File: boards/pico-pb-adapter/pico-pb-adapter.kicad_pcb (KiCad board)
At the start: 2 copper layers, 63.5 x 33 mm, 2 parts, among them U1 RPi_Pico, U2 PocketBeagle

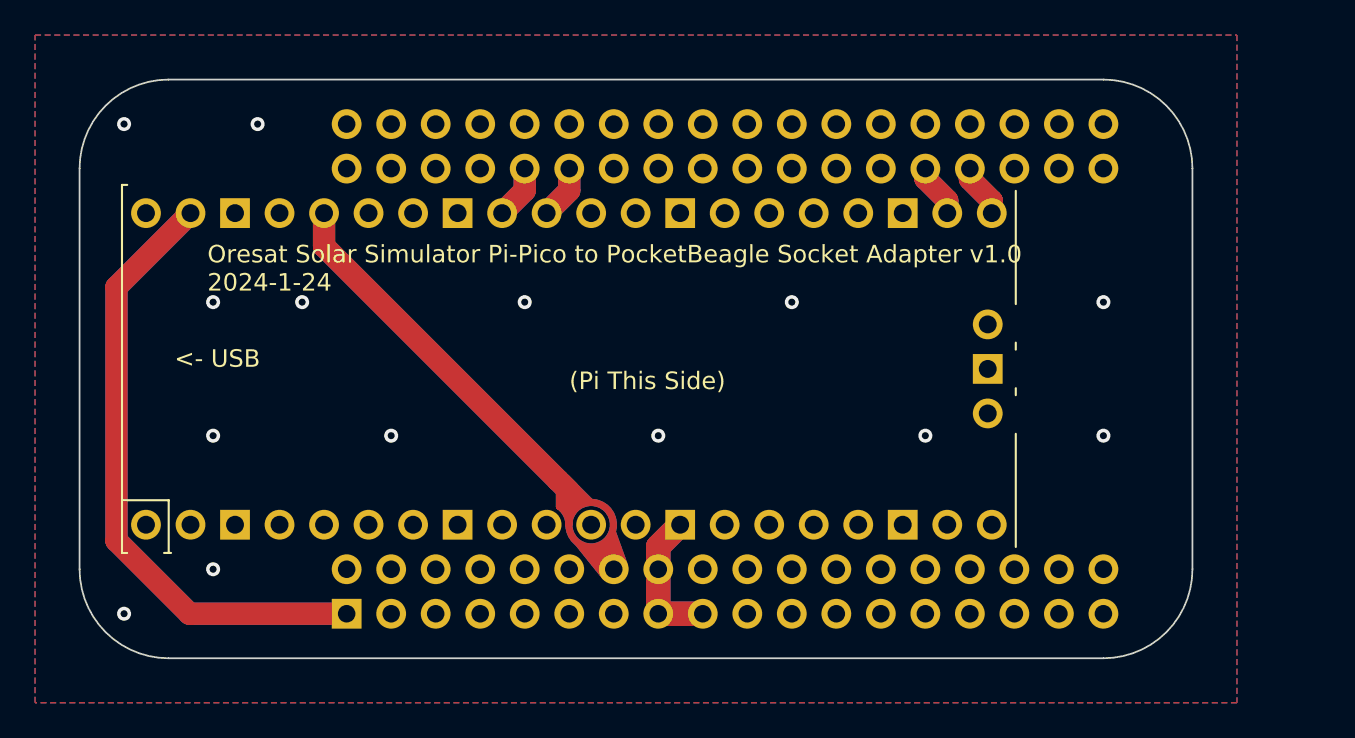
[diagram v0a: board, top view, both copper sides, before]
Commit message: compleded v1.0 adapter for raspberry pi pico to pocket-beagle socket (on solar sim controller board)
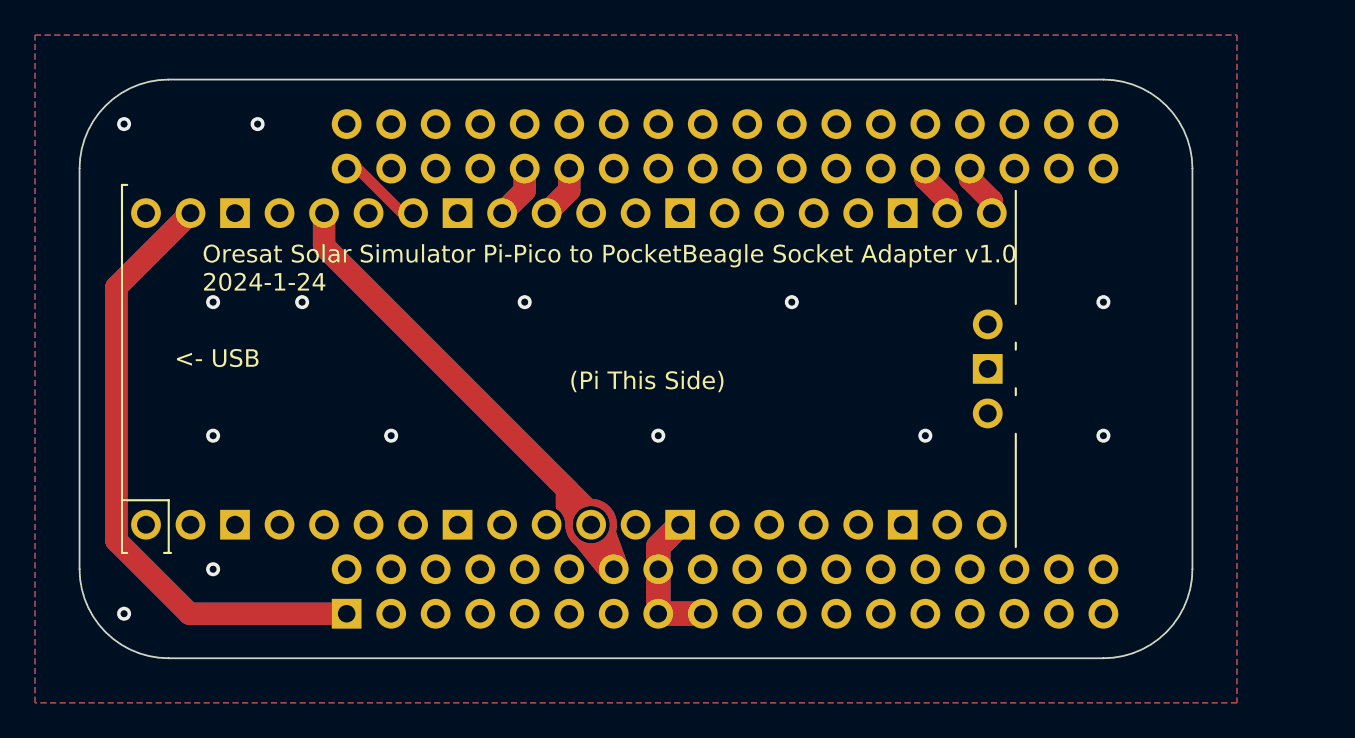
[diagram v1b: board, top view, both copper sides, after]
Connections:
- U1 pad 34: unconnected-(U1-GPIO28_ADC2-Pad34) -> PWM1
- U2 pad 22: GND -> (no net)
- U2 pad 37: unconnected-(U2-PWM1A-Pad37) -> PWM1
- U2 pad 51: GND -> (no net)
- U2 pad 57: GND -> (no net)
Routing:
- net PWM1: track 0.00 -> 9.68 mm

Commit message: Small changes for production, maybe? And upgraded to KiCAD 8.
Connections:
- U1 pad 18: unconnected-(U1-GND-Pad18) -> GND
- U1 pad 23: unconnected-(U1-GND-Pad23) -> GND
- U1 pad 28: unconnected-(U1-GND-Pad28) -> GND
- U1 pad 33: unconnected-(U1-AGND-Pad33) -> GND
- U1 pad 42: unconnected-(U1-GND-Pad42) -> GND
- U2 pad 22: (no net) -> GND
- U2 pad 51: (no net) -> GND
- U2 pad 57: (no net) -> GND
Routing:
- net GND: track 16.3 -> 49.4 mm
